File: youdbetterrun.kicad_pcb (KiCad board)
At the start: 4 copper layers, 60 x 53 mm, 49 parts, among them J201 GT-USB-7010ASV, J301 Conn_01x05_Pin, J302 Conn_01x10_Pin, J401 FH12A-24S-0.5SH(55), Q201 S8050, Q202 S8050, Q401 Q_NMOS_GSD, SW301 TS-1088R-02026, SW302 TS-1088R-02026, U202 CP2104, U301 ESP-12F, U501 SPX3819M5-L-3-3

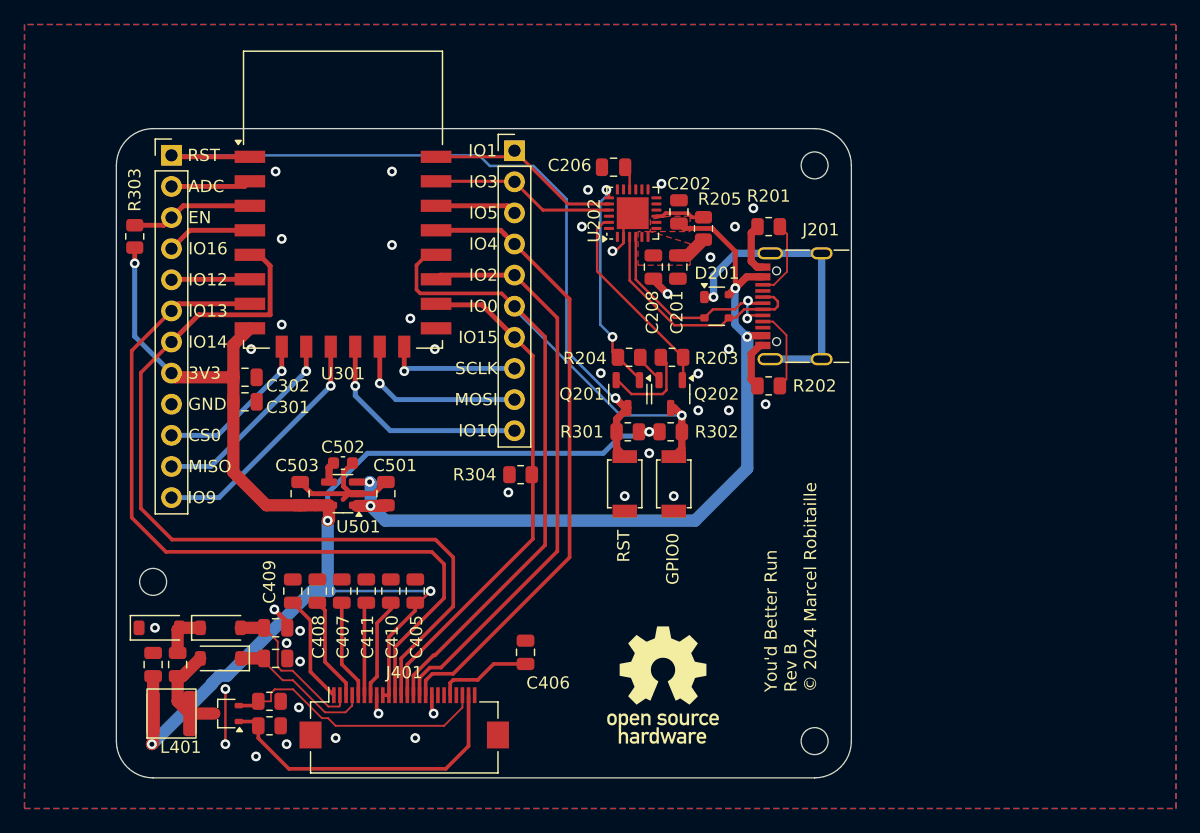
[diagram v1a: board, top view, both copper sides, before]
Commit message: Update layout and routing
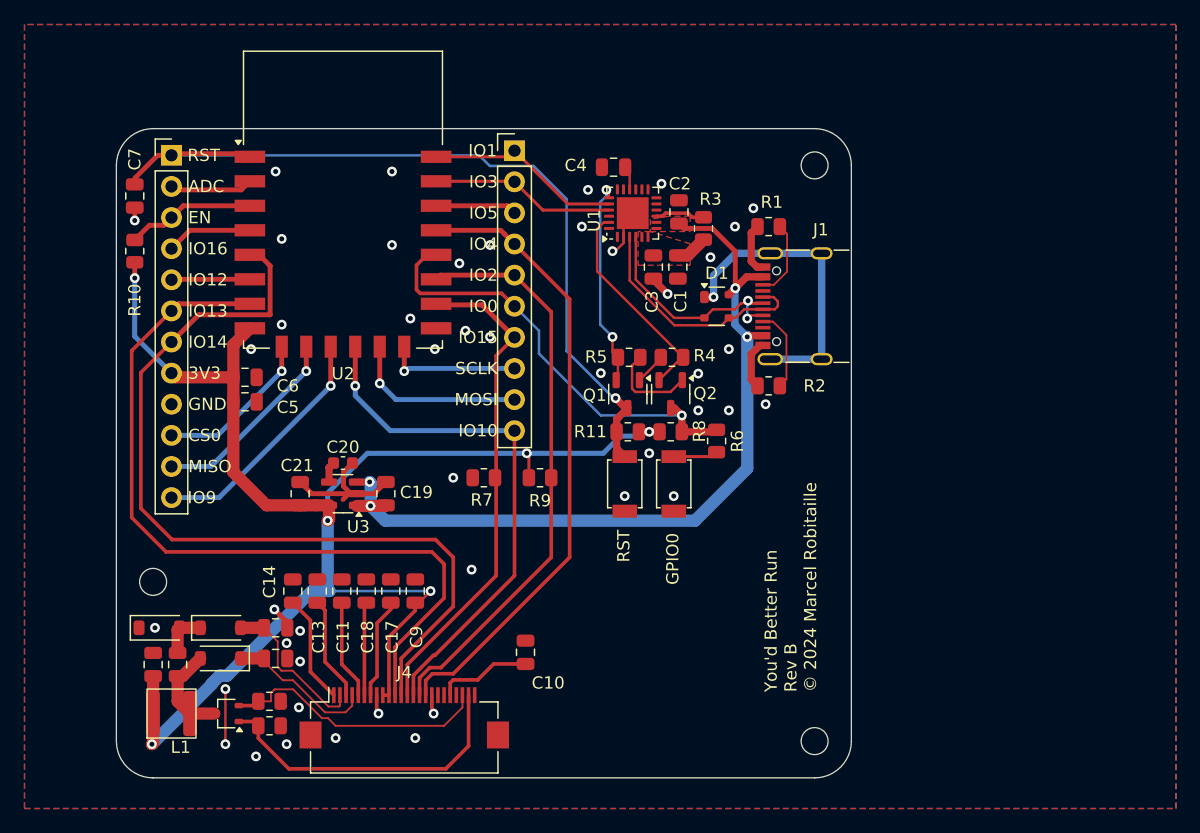
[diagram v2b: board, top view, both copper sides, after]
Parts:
- removed REF**: OSHW_LOGO, youdbetterrun:OSHW_LOGO
- added C7: 470p, Capacitor_SMD:C_0805_2012Metric, F.Cu at (94.0, 59.0)
- added R6: 470, Resistor_SMD:R_0805_2012Metric, F.Cu at (141.5, 79.0)
- added R9: 10k, Resistor_SMD:R_0805_2012Metric, F.Cu at (127.1, 82.0)
- C20: renamed from C502; value 10n -> 10n
- J1: renamed from J201; value GT-USB-7010ASV -> GT-USB-7010ASV
- J4: renamed from J401; value FH12A-24S-0.5SH(55) -> FH12A-24S-0.5SH(55)
- moved R7 3.01 mm to (122.5, 82.0)
- moved R10 1.20 mm to (94.0, 63.5)
- turned SW1 to -90 degrees
- renumbered C201 to C1, C406 to C10, C407 to C11, C403 to C12, C408 to C13, C409 to C14, C401 to C15, C404 to C16, C410 to C17, C411 to C18, C501 to C19, C202 to C2, C503 to C21, C208 to C3, C206 to C4, C301 to C5, C302 to C6, C402 to C8, C405 to C9, D201 to D1, D401 to D2, D403 to D3, D402 to D4, J301 to J2, J302 to J3, L401 to L1, Q201 to Q1, Q202 to Q2, Q401 to Q3, R201 to R1, R303 to R10, R301 to R11, R402 to R12, R401 to R13, R202 to R2, R205 to R3, R203 to R4, R204 to R5, R304 to R7, R302 to R8, SW302 to SW1, SW301 to SW2, U202 to U1, U301 to U2, U501 to U3
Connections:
- J3 pad 10: /MCU/GPIO10 -> /EPD/EPD_D/C
- J3 pad 6: /EPD/EPD_D/C -> /MCU/GPIO0
- Q1 pad 1: /USB/~{RTS} -> Net-(Q1-B)
- Q1 pad 2: Net-(Q201-B) -> /USB/~{RTS}
- Q2 pad 1: /USB/~{DTR} -> Net-(Q2-B)
- Q2 pad 2: Net-(Q202-B) -> /USB/~{DTR}
- Q2 pad 3: /EPD/EPD_D/C -> /MCU/GPIO0
- R4 pad 2: Net-(Q201-B) -> Net-(Q1-B)
- R5 pad 2: Net-(Q202-B) -> Net-(Q2-B)
- R8 pad 2: /EPD/EPD_D/C -> /MCU/GPIO0
- SW1 pad 1: GND -> Net-(R6-Pad1)
- SW1 pad 2: /EPD/EPD_D/C -> GND
- U2 pad 12: /MCU/GPIO10 -> /EPD/EPD_D/C
- U2 pad 18: /EPD/EPD_D/C -> /MCU/GPIO0
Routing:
- net /MCU/GPIO0: track 0.00 -> 36.7 mm, vias 0 -> 1
- net /EPD/EPD_D/C: track 71.8 -> 43.3 mm
- net /MCU/GPIO10: track 18.2 -> 0.00 mm, vias 1 -> 0
- net Net-(Q2-B): track 0.00 -> 7.51 mm
- net Net-(Q201-B): track 7.47 -> 0.00 mm
- net /MCU/~{RST}: track 64.1 -> 68.0 mm
- net Net-(R6-Pad1): track 0.00 -> 3.65 mm
- net Net-(Q1-B): track 0.00 -> 2.58 mm
- net Net-(Q202-B): track 2.54 -> 0.00 mm
- net /EPD/SPI.~{CS}: track 41.6 -> 40.4 mm
- net GND: track 35.7 -> 36.8 mm, vias 40 -> 46
- net /EPD/3V3: track 121.3 -> 122.2 mm, vias 5 -> 6
- net /USB/~{DTR}: track 16.5 -> 17.3 mm
- net /USB/~{RTS}: track 17.8 -> 17.1 mm
